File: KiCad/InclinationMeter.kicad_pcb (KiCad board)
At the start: 4 copper layers, 120 x 80 mm, 108 parts, among them J1 JST_PH_2.0mm_1x02, J2 USB-C, J3 Header_FFC_1.0mm_06, J4 Header_50mil_2x07, J5 Header_FFC_1.0mm_10, J6 Header_FFC_1.0mm_10, Q1 DMG2305UX, Q2 FS8205A, Q3 DMG2305UX, Q4 AO3400A, Q5 AO3400A, SW1 PEC11R-4215F-S0024, SW2 PEC11R-4215F-S0024, U1 DW01A, U10 SN74HC14PWR, U11 LM35DGS, U2 LP5907MFX-3.3/NOPB, U3 TP4056, U4 LP5907MFX-3.3/NOPB, U5 SD6210A, U6 STM32G0B1RET6, U7 RN4871-I_RM128, U8 SN74AHCT244DBR, U9 24LC256-I_ST, Y1 32.768kHz, Y2 8MHz

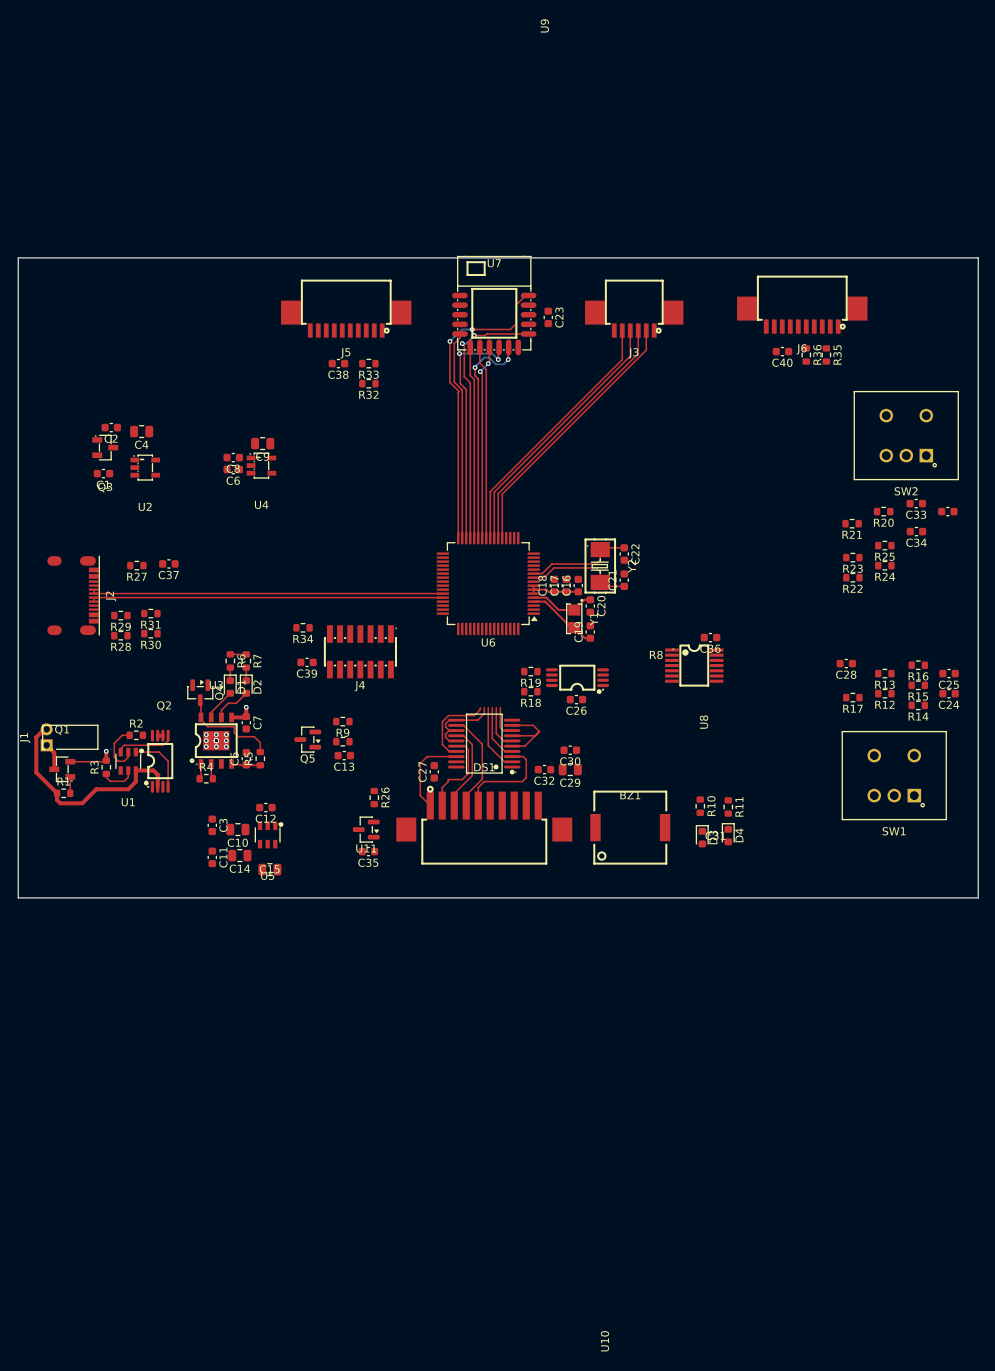
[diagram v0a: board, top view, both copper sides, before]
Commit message: Basic board layout changed. MCU pinout changed accordingly
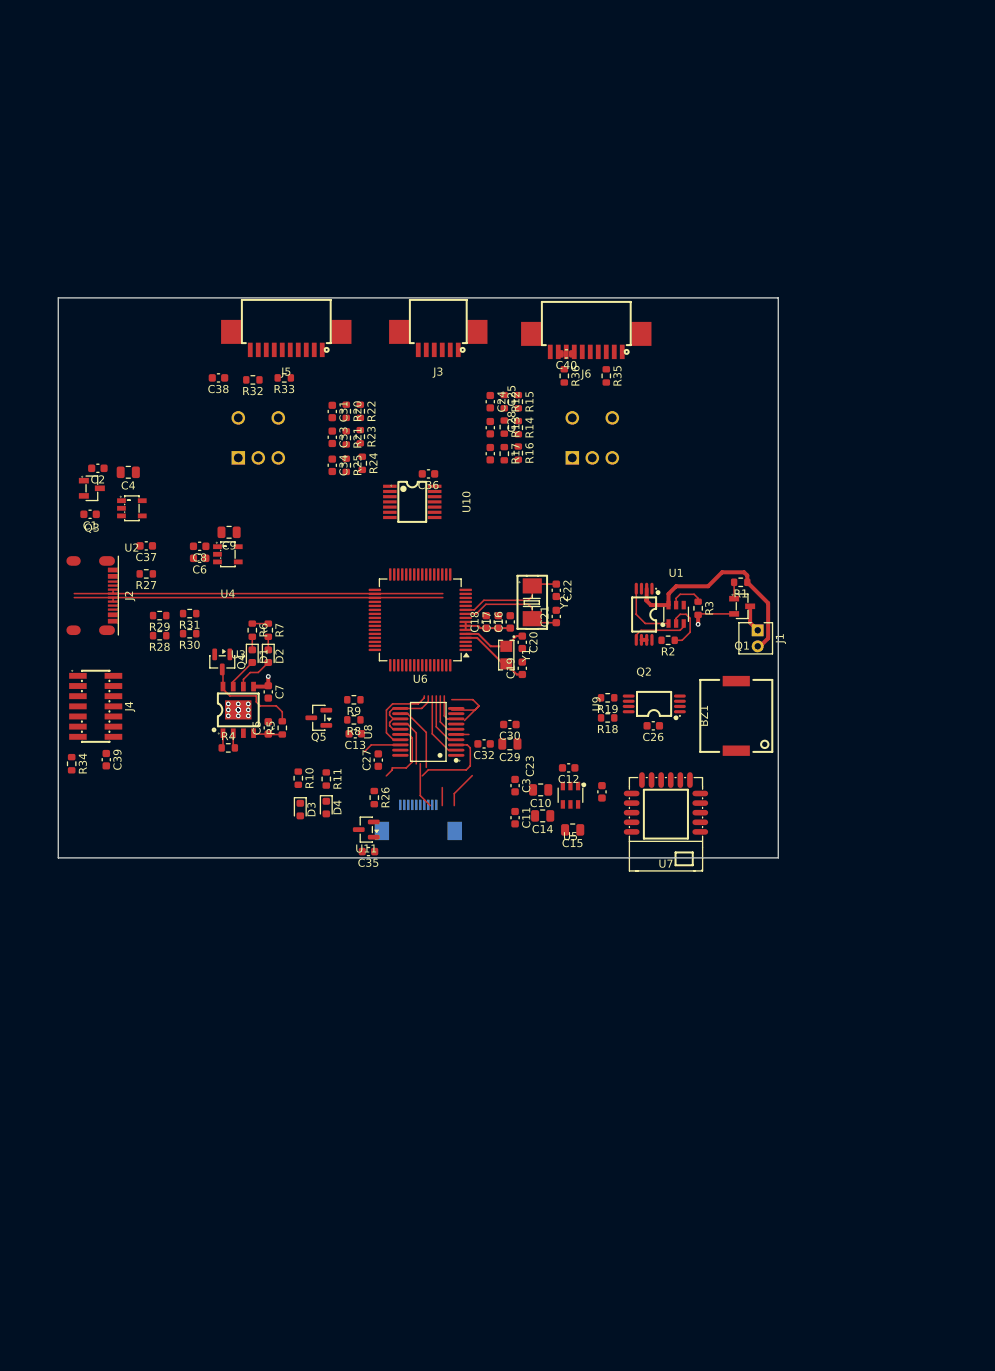
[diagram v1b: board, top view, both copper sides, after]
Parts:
- DS1: footprint sldrnrd:Header_FFC_1.5mm_10 -> sldrnrd:Display_LS027B7DH01; moved to B.Cu
- SW1, SW2: moved to B.Cu
- moved J1 90.0 mm to (137.4, 71.5), turned to -90 degrees
- moved R1 88.6 mm to (135.3, 65.5), turned to 180 degrees
- moved Q1 87.4 mm to (135.5, 68.5), turned to 180 degrees
- moved SW2 81.0 mm to (75.0, 50.0), turned to 0 degrees
- moved C31 78.0 mm to (84.2, 44.2), turned to -90 degrees
- moved R3 76.6 mm to (130.0, 68.8), turned to -90 degrees
- moved C34 73.5 mm to (84.2, 50.9), turned to -90 degrees
- moved C33 73.5 mm to (84.2, 47.4), turned to -90 degrees
- moved U1 70.9 mm to (127.2, 69.5), turned to 0 degrees
- moved R20 68.3 mm to (86.0, 44.2), turned to -90 degrees
- moved R25 68.1 mm to (86.0, 50.9), turned to -90 degrees
- moved C24 68.0 mm to (104.0, 43.0), turned to -90 degrees
- moved R2 67.5 mm to (126.2, 72.8), turned to 180 degrees
- moved R24 66.6 mm to (88.0, 50.7), turned to -90 degrees
- moved C25 65.1 mm to (104.0, 46.2), turned to -90 degrees
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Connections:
- C32 pad 1: DISP_ON_5V -> 5V0
- DS1 pad 11: (no net) -> GND
- DS1 pad 12: (no net) -> GND
- U6 pad 25: BLE_UART_MCU_TO_BLE -> ENC_1B
- U6 pad 26: BLE_UART_BLE_TO_MCU -> ENC_1A
- U6 pad 62: ENC_1B -> BLE_UART_MCU_TO_BLE
- U6 pad 63: ENC_1A -> BLE_UART_BLE_TO_MCU
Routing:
- net BLE_P2_0: track 38.7 -> 0.00 mm, vias 2 -> 0
- net BLE_P0_2: track 33.5 -> 0.00 mm, vias 2 -> 0
- net SCL3300_CS: track 33.4 -> 0.00 mm
- net SCL3300_SCK: track 33.2 -> 0.00 mm
- net SCL3300_MISO: track 33.0 -> 0.00 mm
- net SCL3300_MOSI: track 32.8 -> 0.00 mm
- net BLE_P3_6: track 30.2 -> 0.00 mm, vias 2 -> 0
- net ~{BLE_RST}: track 28.4 -> 0.00 mm, vias 2 -> 0
- net BLE_P1_7: track 26.2 -> 0.00 mm
- net BLE_UART_BLE_TO_MCU: track 24.4 -> 0.00 mm, vias 2 -> 0
- net BLE_UART_MCU_TO_BLE: track 24.2 -> 0.00 mm
- net BLE_P1_6: track 24.1 -> 0.00 mm
- net DISP_VCOM_5V: track 12.7 -> 8.58 mm
- net USB_D-: track 44.1 -> 46.6 mm
- net USB_D+: track 44.1 -> 46.6 mm
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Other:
- board size 120 x 80 mm -> 90 x 70 mm

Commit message: Encoder fixed, main parts and dimensions locked
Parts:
- added H1: MountingHole_Pad, sldrnrd:MountingHole_3.2mm, F.Cu at (136.0, 96.0)
- added H2: MountingHole_Pad, sldrnrd:MountingHole_3.2mm, F.Cu at (54.0, 34.0)
- added H3: MountingHole_Pad, sldrnrd:MountingHole_3.2mm, F.Cu at (136.0, 34.0)
- added H4: MountingHole_Pad, sldrnrd:MountingHole_3.2mm, F.Cu at (54.0, 96.0)
- moved R32 10.8 mm to (64.0, 37.0)
- moved R33 10.7 mm to (68.0, 37.0)
- moved R35 8.39 mm to (126.0, 36.0)
- moved R36 7.75 mm to (106.0, 37.0)
- moved C38 7.63 mm to (67.0, 33.0)
- moved SW2 5.00 mm to (72.0, 46.0), turned to -90 degrees
- moved SW1 4.19 mm to (118.0, 46.0), turned to 90 degrees
- moved R13 3.00 mm to (102.8, 46.2)
- moved R16 3.00 mm to (104.5, 49.5)
- moved C24 3.00 mm to (101.0, 43.0)
- moved C25 3.00 mm to (101.0, 46.2)
- moved C28 3.00 mm to (101.0, 49.5)
- moved R12 3.00 mm to (102.8, 43.0)
- moved R14 3.00 mm to (104.5, 46.2)
- moved R15 3.00 mm to (104.5, 43.0)
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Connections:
- U6 pad 1: ENC_2B -> ~{BLE_RST}
- U6 pad 17: unconnected-(U6-PA0-Pad17) -> ENC_1SW
- U6 pad 2: ENC_2A -> BLE_P1_6
- U6 pad 25: ENC_1B -> ENC_1A
- U6 pad 26: ENC_1A -> ENC_2SW
- U6 pad 27: ~{BLE_RST} -> ENC_1B
- U6 pad 28: BLE_P1_6 -> ENC_2A
- U6 pad 29: BLE_P0_2 -> ENC_2B
- U6 pad 3: ENC_2SW -> BLE_P2_0
- U6 pad 30: BLE_P3_6 -> unconnected-(U6-PB10-Pad30)
- U6 pad 31: BLE_P1_7 -> LED_STATUS
- U6 pad 32: BLE_P2_0 -> LED_PWR
- U6 pad 58: LED_STATUS -> BLE_P0_2
- U6 pad 59: ENC_1SW -> BLE_P1_7
- U6 pad 64: LED_PWR -> BLE_P3_6
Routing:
- net DISP_SCK_5V: track 10.6 -> 4.87 mm
- net DISP_CS_5V: track 11.0 -> 6.33 mm
- net DISP_MOSI_5V: track 11.0 -> 8.79 mm
- net ~{ENC_1SW_RAW}: track 0.00 -> 1.77 mm
- net ~{ENC_1B_RAW}: track 0.00 -> 1.77 mm
- net ~{ENC_1A_RAW}: track 0.00 -> 1.77 mm
- net Net-(SW1-SW1): track 0.00 -> 1.75 mm
- net Net-(SW1-B): track 0.00 -> 1.75 mm
- net Net-(SW1-A): track 0.00 -> 1.75 mm
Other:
- outline, holes or cut-outs redrawn

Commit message: Board largely routed, except power and gnd
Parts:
- added C41: 100n, sldrnrd:C_0603, F.Cu at (98.3, 39.5)
- moved C8 65.7 mm to (132.0, 47.5), turned to 0 degrees
- moved C1 65.0 mm to (117.0, 73.0), turned to 0 degrees
- moved C6 64.2 mm to (131.5, 55.8), turned to 0 degrees
- moved C2 64.0 mm to (117.5, 65.0), turned to 0 degrees
- moved U4 61.5 mm to (132.0, 52.8), turned to -90 degrees
- moved C9 61.4 mm to (132.0, 49.5), turned to 0 degrees
- moved Q3 61.1 mm to (114.0, 66.2), turned to -90 degrees
- moved C4 60.7 mm to (117.5, 67.0), turned to 0 degrees
- moved U2 59.9 mm to (117.5, 70.2), turned to -90 degrees
- moved BZ1 53.1 mm to (82.5, 91.5), turned to -90 degrees
- moved D3 34.5 mm to (78.0, 58.2), turned to 180 degrees
- moved C3 34.2 mm to (132.2, 67.8), turned to 0 degrees
- moved D4 32.4 mm to (78.0, 60.2), turned to 180 degrees
- moved R10 30.8 mm to (81.2, 58.2), turned to 180 degrees
- moved C35 29.3 mm to (77.5, 70.0)
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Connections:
- C32 pad 1: 5V0 -> DISP_ON_5V
- U10 pad 1: ~{ENC_1A_RAW} -> ~{ENC_1SW_RAW}
- U10 pad 2: ENC_1A -> ENC_1SW
- U10 pad 3: ~{ENC_1B_RAW} -> ~{ENC_1A_RAW}
- U10 pad 4: ENC_1B -> ENC_1A
- U10 pad 5: ~{ENC_1SW_RAW} -> ~{ENC_1B_RAW}
- U10 pad 6: ENC_1SW -> ENC_1B
- U6 pad 1: ~{BLE_RST} -> BLE_P2_0
- U6 pad 2: BLE_P1_6 -> ~{BLE_RST}
- U6 pad 20: ~{CHARGE_EN} -> CHARGE_SENSE
- U6 pad 3: BLE_P2_0 -> BLE_P1_6
- U6 pad 35: PCAP04_1_P2 -> PCAP04_1_P3
- U6 pad 36: PCAP04_1_P3 -> PCAP04_1_P2
- U6 pad 56: CHARGE_SENSE -> ~{CHARGE_EN}
- U8 pad 10: unconnected-(U8-GND-Pad10) -> GND
- U8 pad 12: DISP_VCOM_5V -> DISP_MOSI_5V
- U8 pad 16: DISP_MOSI_5V -> DISP_VCOM_5V
- U8 pad 17: DISP_ON -> DISP_SCK
- U8 pad 18: DISP_SCK_5V -> DISP_ON_5V
- U8 pad 2: DISP_SCK -> DISP_ON
- U8 pad 3: DISP_ON_5V -> DISP_SCK_5V
- U8 pad 4: DISP_MOSI -> DISP_VCOM
- U8 pad 8: DISP_VCOM -> DISP_MOSI
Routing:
- net 3V3_Sensors: track 0.00 -> 97.1 mm
- net ~{RST}: track 0.00 -> 55.3 mm
- net SWO: track 0.00 -> 49.1 mm, vias 0 -> 2
- net VBUS_SENSE: track 0.00 -> 48.9 mm, vias 0 -> 2
- net CHARGE_SENSE: track 4.00 -> 51.0 mm, vias 0 -> 2
- net DEBUG_UART_MCU_TO_PC: track 0.00 -> 42.7 mm, vias 0 -> 2
- net BLE_P1_7: track 0.00 -> 42.6 mm, vias 0 -> 2
- net DEBUG_UART_PC_TO_MCU: track 0.00 -> 42.3 mm, vias 0 -> 2
- net BLE_P2_0: track 0.00 -> 40.6 mm, vias 0 -> 2
- net 5V0: track 0.00 -> 40.2 mm, vias 0 -> 3
- net BLE_UART_MCU_TO_BLE: track 0.00 -> 39.4 mm
- net PCAP04_2_SCL: track 0.00 -> 39.0 mm
- net EEPROM_SCL: track 0.00 -> 38.3 mm, vias 0 -> 2
- net BLE_UART_BLE_TO_MCU: track 0.00 -> 37.7 mm
- net EEPROM_SDA: track 0.00 -> 37.6 mm, vias 0 -> 2
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
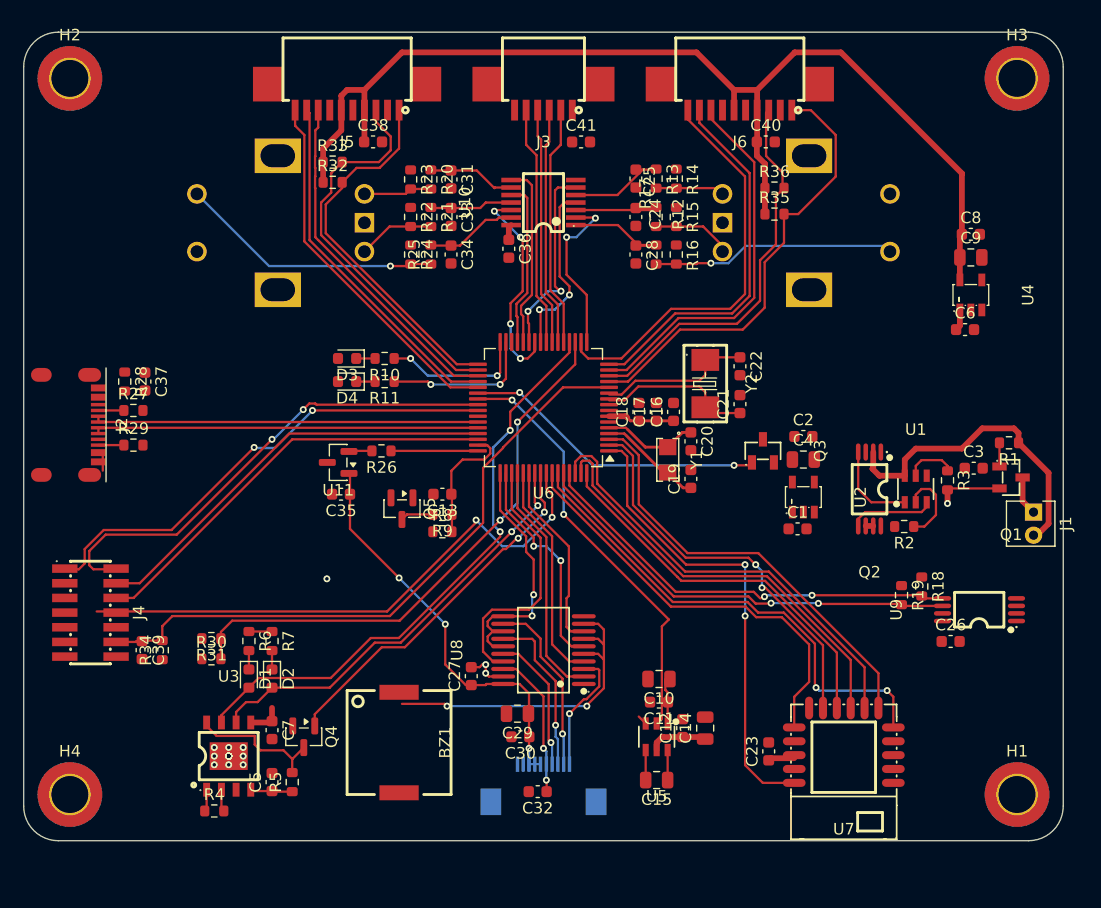
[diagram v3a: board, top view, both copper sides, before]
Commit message: Environmental sensor added, mostly routed.
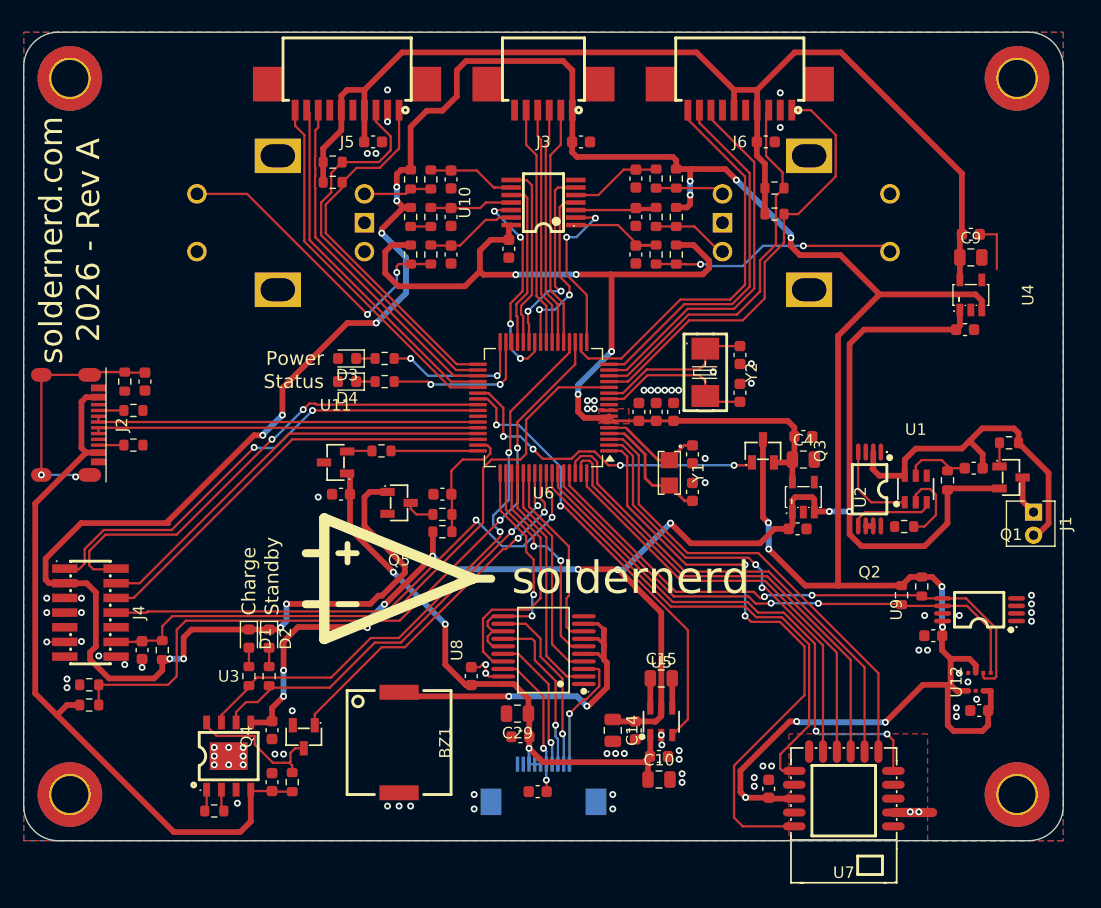
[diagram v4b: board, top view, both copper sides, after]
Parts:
- added C42: 100n, sldrnrd:C_0603, F.Cu at (132.7, 88.7)
- added U12: BME280, sldrnrd:LGA-8_2.5x2.5mm_P0.65mm, F.Cu at (132.8, 86.2)
- Q1, Q3: footprint sldrnrd:SOT-23-BR -> sldrnrd:SOT-23-3
- Q4, Q5, U11: footprint sldrnrd:SOT-23 -> sldrnrd:SOT-23-3
- moved R30 11.3 mm to (55.7, 88.2)
- moved R31 11.3 mm to (55.7, 86.5)
- moved C15 8.81 mm to (105.2, 86.0), turned to 0 degrees
- moved C10 8.70 mm to (105.0, 94.7), turned to 0 degrees
- moved C14 8.00 mm to (101.0, 90.5), turned to -90 degrees
- moved C11 4.70 mm to (105.0, 92.7), turned to 0 degrees
- moved C12 4.10 mm to (103.0, 90.5), turned to -90 degrees
- moved U7 3.77 mm to (121.0, 95.5)
- moved D2 3.47 mm to (71.2, 82.5)
- moved D1 3.46 mm to (69.5, 82.5)
- moved C23 3.23 mm to (114.5, 95.5)
- moved R7 3.05 mm to (71.2, 85.8)
- moved R6 3.04 mm to (69.5, 85.8)
- moved C26 1.58 mm to (128.8, 82.2), turned to 180 degrees
- moved U5 1.36 mm to (105.2, 89.7), turned to 0 degrees
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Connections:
- D1 pad 1: Net-(D1-A) -> 3V3
- D1 pad 2: CHARGE_SENSE -> Net-(D1-K)
- D2 pad 1: Net-(D2-A) -> 3V3
- D2 pad 2: STANDBY_SENSE -> Net-(D2-K)
- R6 pad 1: 3V3 -> Net-(D1-K)
- R6 pad 2: Net-(D1-A) -> CHARGE_SENSE
- R7 pad 1: 3V3 -> Net-(D2-K)
- R7 pad 2: Net-(D2-A) -> STANDBY_SENSE
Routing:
- net 3V3: track 4.29 -> 296.2 mm, vias 0 -> 21
- net VCC: track 15.7 -> 134.8 mm, vias 1 -> 10
- net 3V3_STANDBY: track 7.43 -> 82.8 mm, vias 0 -> 4
- net V_USB: track 3.66 -> 62.9 mm
- net Net-(C37-Pad1): track 0.00 -> 22.1 mm, vias 0 -> 2
- net VBUS_SENSE: track 48.9 -> 63.1 mm
- net EEPROM_SDA: track 37.6 -> 49.1 mm
- net BLE_P2_0: track 40.6 -> 51.9 mm
- net 5V0: track 40.2 -> 50.8 mm
- net GND: track 6.78 -> 15.9 mm, vias 22 -> 82
- net EEPROM_SCL: track 38.3 -> 47.1 mm
- net BLE_P0_2: track 36.9 -> 42.2 mm
- net Net-(SW2-B): track 6.65 -> 1.75 mm
- net Net-(SW2-SW1): track 22.9 -> 27.6 mm, vias 1 -> 2
- net BLE_UART_BLE_TO_MCU: track 37.7 -> 41.4 mm
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- added copper zone on F.Cu, net 3V3_STANDBY
- added copper zone on B.Cu, net GND
- added copper zone on F.Cu, net GND
- added copper zone on In2.Cu, net GND
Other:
- board text added: "Charge"
- board text added: "Power"
- board text added: "Standby"
- board text added: "Status"
- board text added: "soldernerd"
- board text added: "soldernerd.com 2026 - Rev A"

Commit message: Routed with no errors, silkscreen done
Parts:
- moved J3 2.00 mm to (95.0, 33.0)
- moved J5 2.00 mm to (78.0, 33.0)
- moved J6 2.00 mm to (112.0, 33.0)
- moved J1 1.20 mm to (137.4, 72.8)
- moved C36 1.06 mm to (91.2, 48.0), turned to 180 degrees
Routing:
- net Net-(SW2-B): track 1.75 -> 6.65 mm
- net GND: track 15.9 -> 11.0 mm, vias 82 -> 221
- net PCAP04_1_SDA: track 34.1 -> 32.0 mm
- net 3V3_STANDBY: track 82.8 -> 81.2 mm
- net BAT-: track 30.5 -> 32.2 mm
- net BAT+: track 3.39 -> 4.59 mm
- net VCC: track 134.8 -> 135.8 mm
- net BUZZER_5V: track 30.2 -> 31.1 mm
- net DISP_SCK_5V: track 10.7 -> 11.4 mm
- net 5V_EN: track 39.0 -> 39.6 mm
- net 3V3: track 296.2 -> 296.5 mm, vias 21 -> 20
